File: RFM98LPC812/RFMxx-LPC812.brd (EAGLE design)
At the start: 60 x 40 mm, 21 parts, among them X1 BU-SMA-V, X2 BU-SMA-V

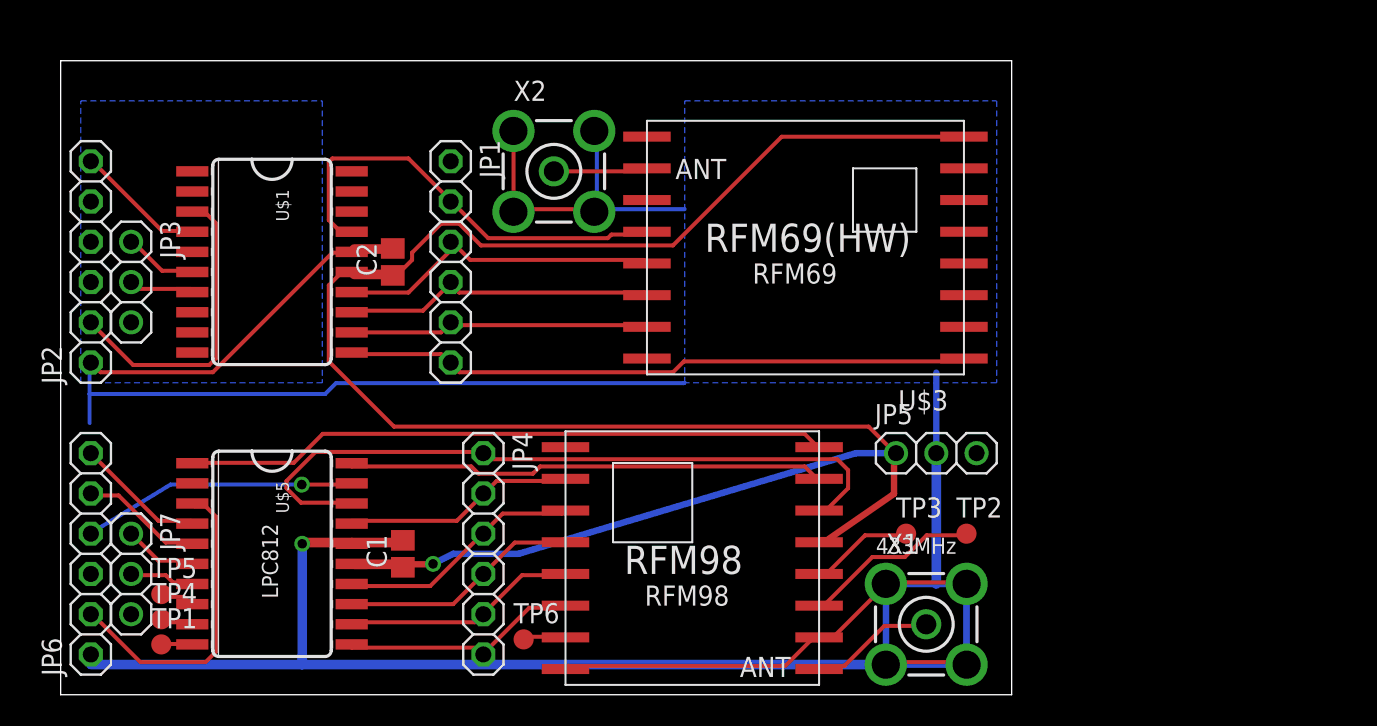
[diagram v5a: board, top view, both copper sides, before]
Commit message: LEDs on DIO0
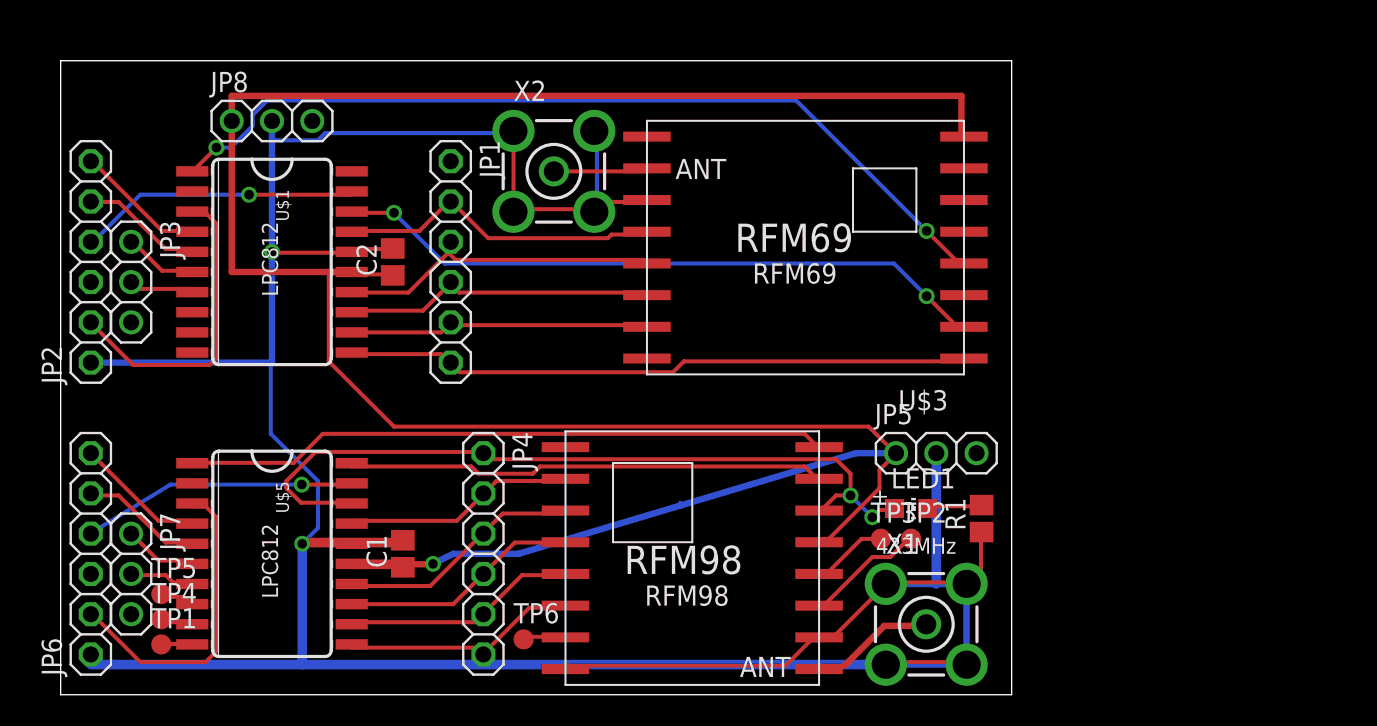
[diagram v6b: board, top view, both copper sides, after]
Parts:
- added JP8: (no value), adafruit:1X03
- added LED1: (no value), adafruit:CHIP-LED0805
- added R1: (no value), resistor:R0805
- moved TP2 3.51 mm to (53.7, 9.84)
- moved TP3 1.62 mm to (51.8, 9.84)
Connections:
- new net N$2: JP2.5, U$1.5
- new net N$24: U$1.18, U$3.DIO0
- new net N$35: JP2.4, U$1.19
- new net N$36: U$1.1, U$3.DIO2
- new net N$37: LED1.C, R1.2
- net GND: now also JP8.2, R1.1, U$3.GND
- net N$22: now also LED1.A
- net VCC: now also JP8.1
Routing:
- net N$36: track 0.00 -> 55.3 mm, vias 0 -> 2
- net N$24: track 0.00 -> 41.6 mm, vias 0 -> 2
- net VCC: track 132.7 -> 157.8 mm
- net N$35: track 0.00 -> 17.8 mm, vias 0 -> 1
- net GND: track 218.1 -> 208.7 mm, vias 1 -> 2
- net N$2: track 0.00 -> 7.75 mm
- net N$19: track 27.8 -> 20.5 mm
- net N$22: track 45.2 -> 49.3 mm, vias 0 -> 2
- net N$30: track 11.3 -> 7.66 mm
- net N$37: track 0.00 -> 3.49 mm
- net N$31: track 6.55 -> 4.82 mm
- removed copper zone on layer 16, net GND
- removed copper zone on layer 16, net N$2
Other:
- board text added: "RFM69"
- board text removed: "RFM69(HW)"

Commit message: trace bug fixes
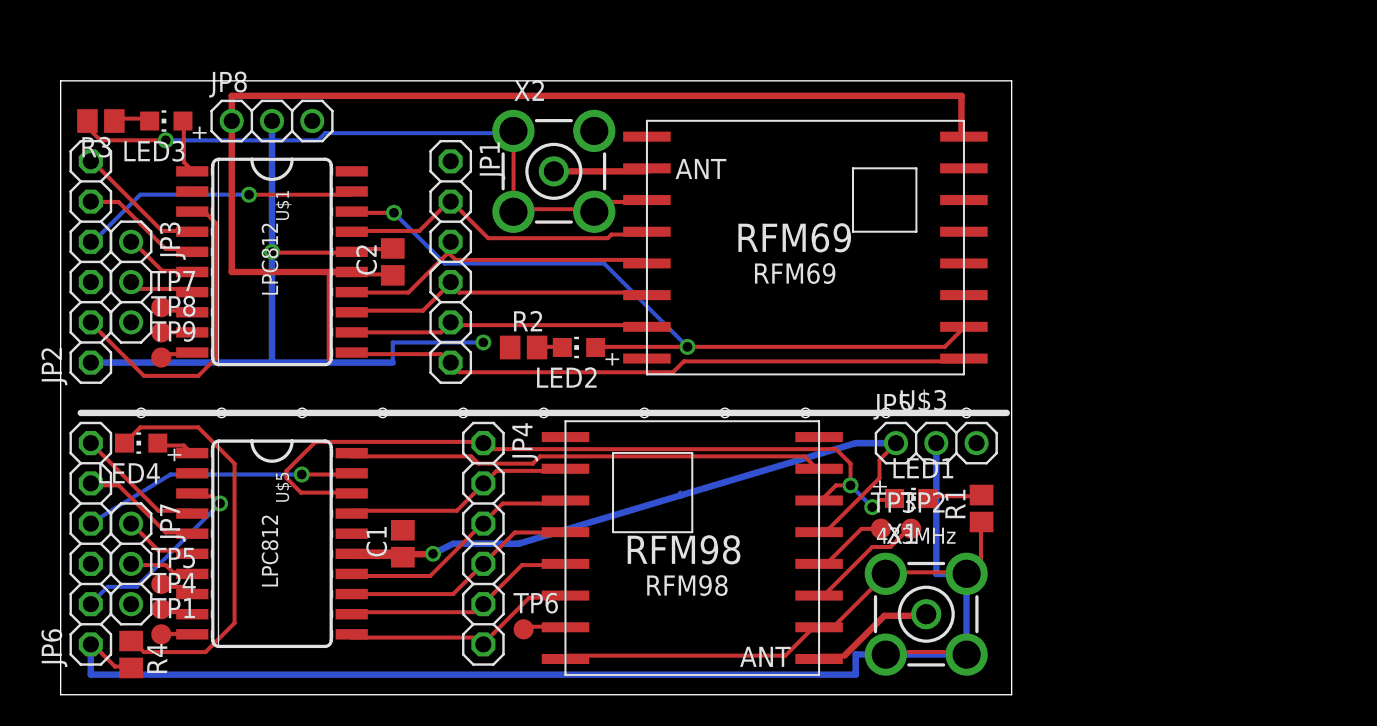
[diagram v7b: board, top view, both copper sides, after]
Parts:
- added LED2, LED3, LED4: (no value), adafruit:CHIP-LED0805
- added R2, R3, R4: 3K3, resistor:R0805
- added TP7, TP8, TP9: TPB1,27, testpad:B1,27
- R1: value (none) -> 3K3
- moved JP7 0.64 mm to (4.45, 8.26)
- moved TP5 0.64 mm to (6.35, 6.99)
- moved U$2 0.64 mm to (39.9, 8.26)
- moved U$5 0.64 mm to (13.3, 8.26)
- moved TP1 0.64 mm to (6.35, 3.81)
- moved TP6 0.64 mm to (29.2, 4.13)
- moved C1 0.63 mm to (21.6, 9.53)
- moved JP4 0.63 mm to (26.7, 9.53)
- moved JP5 0.63 mm to (55.2, 15.9)
- moved JP6 0.63 mm to (1.91, 9.53)
- moved LED1 0.63 mm to (53.7, 12.4)
- moved R1 0.63 mm to (58.1, 11.7)
- moved TP2 0.63 mm to (53.7, 10.5)
- moved TP3 0.63 mm to (51.8, 10.5)
- moved TP4 0.63 mm to (6.35, 5.40)
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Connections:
- new net N$38: LED2.C, R2.2
- new net N$39: LED3.C, R3.1
- new net N$41: TP7.TP, U$1.8
- new net N$42: LED4.C, R4.1
- new net N$43: TP8.TP, U$1.9
- new net N$44: TP9.TP, U$1.10
- net GND: now also R2.1, R3.2, R4.2
- net N$24: now also LED2.A
- net N$26: now also LED4.A; no longer U$2.DIO2
- net N$36: now also LED3.A; no longer U$3.DIO2
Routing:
- net N$36: track 55.3 -> 3.40 mm, vias 2 -> 0
- net N$26: track 40.7 -> 2.49 mm
- net VCC: track 157.8 -> 119.8 mm
- net N$42: track 0.00 -> 25.9 mm
- net N$21: track 19.8 -> 12.8 mm, vias 0 -> 1
- net N$24: track 41.6 -> 48.5 mm
- net GND: track 208.7 -> 205.9 mm
- net N$39: track 0.00 -> 2.42 mm
- net N$41: track 0.00 -> 2.18 mm
- net N$44: track 0.00 -> 2.18 mm
- net N$43: track 0.00 -> 1.96 mm
- net N$38: track 0.00 -> 1.83 mm
- net N$4: track 19.5 -> 20.1 mm
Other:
- board size 60 x 40 mm -> 60 x 38.7 mm

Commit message: attempting to separate vcc, gnd on both sides of the board
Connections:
- new net N$45: C1.2, U$5.16
- net GND: no longer C1.2, U$5.16
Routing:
- net GND: track 205.9 -> 214.8 mm
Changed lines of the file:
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@@
 <text x="42.545" y="27.94" size="1.778" layer="21">RFM69</text>
 <text x="12.7" y="29.845" size="1.016" layer="21" rot="R270">LPC812</text>
-<wire x1="1.27" y1="17.78" x2="59.69" y2="17.78" width="0.4064" layer="21"/>
-<hole x="5.08" y="17.78" drill="0.6"/>
-<hole x="10.16" y="17.78" drill="0.6"/>
-<hole x="15.24" y="17.78" drill="0.6"/>
-<hole x="20.32" y="17.78" drill="0.6"/>
-<hole x="25.4" y="17.78" drill="0.6"/>
-<hole x="30.48" y="17.78" drill="0.6"/>
-<hole x="36.83" y="17.78" drill="0.6"/>
-<hole x="41.91" y="17.78" drill="0.6"/>
-<hole x="46.99" y="17.78" drill="0.6"/>
-<hole x="52.07" y="17.78" drill="0.6"/>
-<hole x="57.15" y="17.78" drill="0.6"/>
+<wire x1="1.27" y1="18.415" x2="59.69" y2="18.415" width="0.4064" layer="21"/>
+<hole x="5.08" y="18.415" drill="0.6"/>
+<hole x="10.16" y="18.415" drill="0.6"/>
+<hole x="15.24" y="18.415" drill="0.6"/>
+<hole x="20.32" y="18.415" drill="0.6"/>
+<hole x="25.4" y="18.415" drill="0.6"/>
+<hole x="30.48" y="18.415" drill="0.6"/>
+<hole x="36.83" y="18.415" drill="0.6"/>
+<hole x="41.91" y="18.415" drill="0.6"/>
+<hole x="46.99" y="18.415" drill="0.6"/>
+<hole x="52.07" y="18.415" drill="0.6"/>
+<hole x="57.15" y="18.415" drill="0.6"/>
 </plain>
 <attributes>
@@
 <wire x1="48.006" y1="10.4648" x2="47.85" y2="10.255" width="0.254" layer="1"/>
 <wire x1="52.578" y1="15.7226" x2="52.705" y2="15.875" width="0.254" layer="1"/>
-<wire x1="46.1772" y1="19.6596" x2="51.6636" y2="14.8082" width="0" layer="19" extent="1-16"/>
-<wire x1="18.288" y1="19.6596" x2="46.1772" y2="19.6596" width="0" layer="19" extent="1-16"/>
-<wire x1="16.9164" y1="21.0312" x2="18.288" y2="19.6596" width="0" layer="19" extent="1-16"/>
+<wire x1="18.3642" y1="8.89" x2="16.9164" y2="21.0312" width="0" layer="19" extent="1-1"/>
 </signal>
 <signal name="N$6">
@@
 <contactref element="U$2" pad="GND2"/>
 <contactref element="U$2" pad="GND3"/>
-<contactref element="C1" pad="2"/>
-<contactref element="U$5" pad="16"/>
 <wire x1="48.768" y1="4.2926" x2="47.8536" y2="4.2926" width="0.254" layer="1"/>
 <wire x1="51.9684" y1="7.493" x2="48.768" y2="4.2926" width="0.254" layer="1"/>
@@
 <wire x1="57.15" y1="2.54" x2="50.165" y2="2.54" width="0.4064" layer="16"/>
 <wire x1="50.165" y1="2.54" x2="50.165" y2="1.27" width="0.4064" layer="16"/>
-<wire x1="50.165" y1="1.27" x2="1.905" y2="1.27" width="0.4064" layer="16"/>
+<wire x1="50.165" y1="1.27" x2="15.24" y2="1.27" width="0.4064" layer="16"/>
+<wire x1="15.24" y1="1.27" x2="1.905" y2="1.27" width="0.4064" layer="16"/>
 <wire x1="1.905" y1="2.54" x2="1.905" y2="3.175" width="0.4064" layer="16"/>
 <wire x1="1.905" y1="1.27" x2="1.905" y2="3.175" width="0.4064" layer="16"/>
 <contactref element="R4" pad="2"/>
+<wire x1="15.24" y1="1.27" x2="15.24" y2="10.16" width="0.4064" layer="16"/>
 <wire x1="34.29" y1="31.0896" x2="33.8328" y2="35.433" width="0" layer="19" extent="1-16"/>
 <wire x1="28.36" y1="21.9075" x2="26.67" y2="22.225" width="0" layer="19" extent="1-16"/>
-<wire x1="21.59" y1="10.375" x2="20.955" y2="20.955" width="0" layer="19" extent="1-16"/>
-<wire x1="18.3642" y1="10.16" x2="21.59" y2="10.375" width="0" layer="19" extent="1-1"/>
-<wire x1="31.8516" y1="2.4638" x2="21.59" y2="10.375" width="0" layer="19" extent="1-1"/>
-<wire x1="57.15" y1="7.62" x2="57.1599" y2="7.6299" width="0" layer="19" extent="16-16"/>
+<wire x1="15.24" y1="10.16" x2="13.335" y2="20.955" width="0" layer="19" extent="16-16"/>
 <wire x1="57.1599" y1="2.5301" x2="57.15" y2="2.54" width="0" layer="19" extent="16-16"/>
+<wire x1="57.1599" y1="7.6299" x2="57.15" y2="7.62" width="0" layer="19" extent="16-16"/>
 <wire x1="4.445" y1="1.69" x2="4.3434" y2="1.778" width="0" layer="19" extent="1-1"/>
 </signal>
@@
 <signal name="N$40">
 <via x="26.67" y="22.225" extent="1-16" drill="0.6"/>
-<wire x1="26.67" y1="22.225" x2="27.94" y2="22.225" width="0" layer="19" extent="1-16"/>
 </signal>
 <signal name="N$42">
@@
 <wire x1="8.2296" y1="21.4884" x2="8.3058" y2="21.59" width="0.254" layer="1"/>
 </signal>
+<signal name="N$45">
+<contactref element="C1" pad="2"/>
+<contactref element="U$5" pad="16"/>
+<wire x1="18.3642" y1="10.16" x2="21.59" y2="10.375" width="0" layer="19" extent="1-1"/>
+</signal>
 </signals>
